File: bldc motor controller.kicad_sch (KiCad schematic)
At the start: 56 parts, among them J1 Conn_01x04_Pin, U1 C47023655, U2 ISM330DHCXTR, U3 C529358, U6 LIS2MDLTR

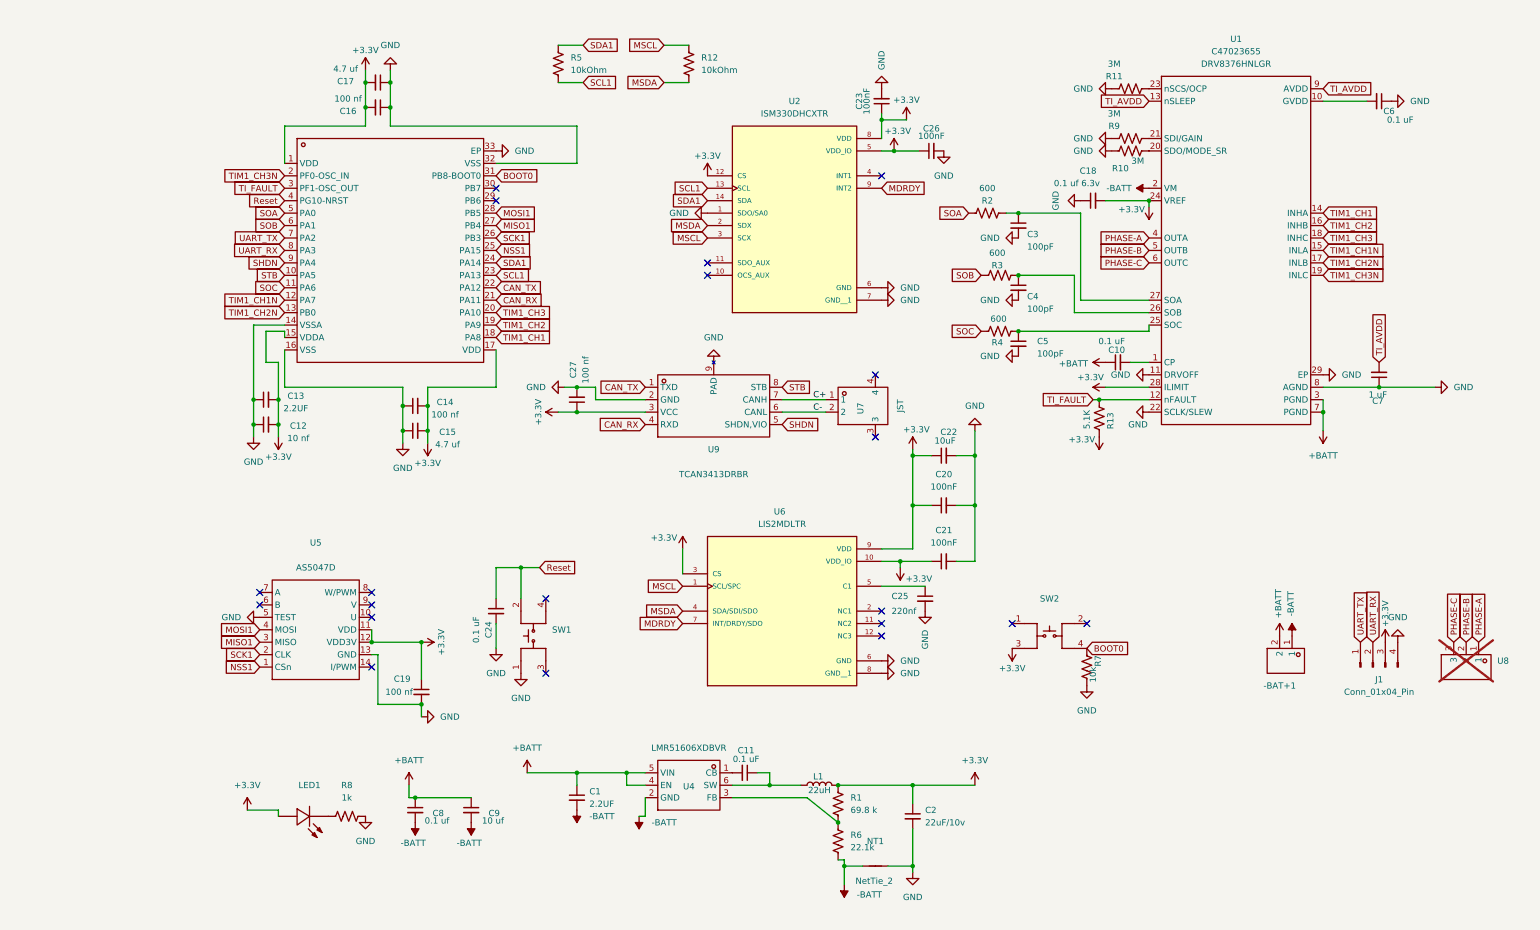
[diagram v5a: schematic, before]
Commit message: updated to min capacitor size and increased width of 3.3v rail
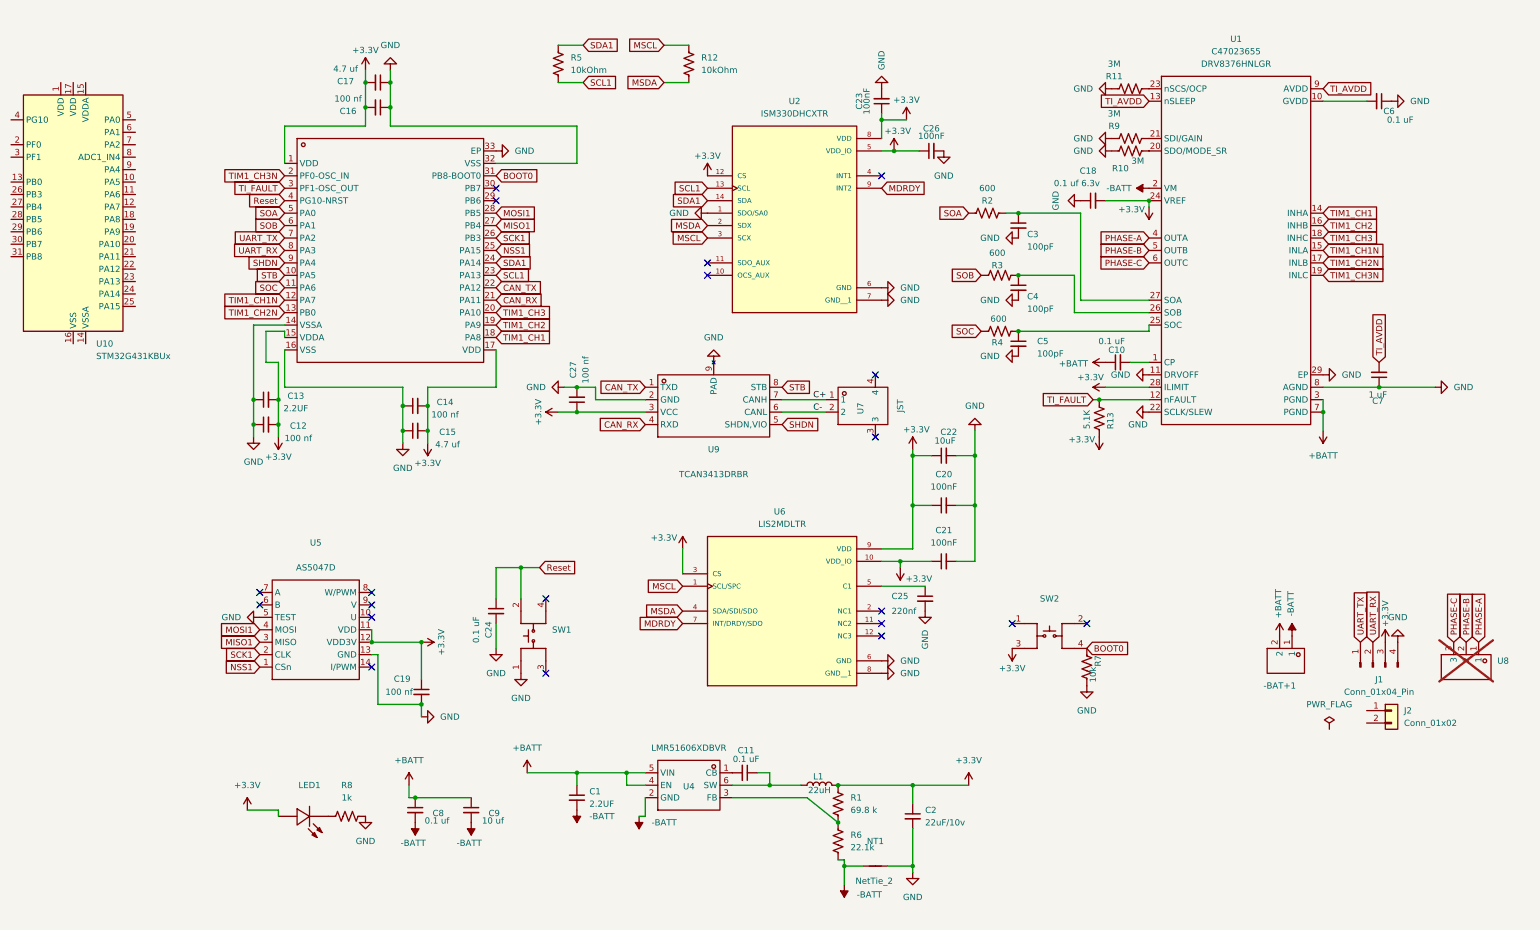
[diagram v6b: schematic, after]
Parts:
- added J2: Conn_01x02, symbol Connector_Generic:Conn_01x02
- added U10: STM32G431KBUx, Package_DFN_QFN:QFN-32-1EP_5x5mm_P0.5mm_EP3.45x3.45mm, symbol MCU_ST_STM32G4:STM32G431KBUx
- C12: value 10 nf -> 100 nf; footprint Capacitor_SMD:C_01005_0402Metric -> Capacitor_SMD:C_0201_0603Metric
- C14, C16, C19, C20, C21, C23, C26, C27, C3, C4, C5: footprint Capacitor_SMD:C_01005_0402Metric -> Capacitor_SMD:C_0201_0603Metric
- C25: footprint Capacitor_SMD:C_01005_0402Metric -> Capacitor_SMD:C_0402_1005Metric
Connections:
- new net: U10.16 (VSS), U10.32 (VSS), U10.33 (VSS)

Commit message: 3.3v plane, finale besides that
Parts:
- removed -BAT+1: ~, Connector_JST:JST_EH_B2B-EH-A_1x02_P2.50mm_Vertical, symbol bldc controller:WAFER-XH254WZ-2AM
- removed U2: ISM330DHCXTR, bldc-motor-footprints:PQFN50P250X300X86-14N, symbol bldc controller:ISM330DHCXTR
- removed U3: C529358, bldc-motor-footprints:QFN-32_L5.0-W5.0-P0.50-BL-EP3.7, symbol bldc controller:STM32G431KBU6
- added C28, C29, C30: 10 uf, Capacitor_SMD:C_0603_1608Metric, symbol Device:C_Small
- added U2: LSM6DSV16XTR, LGA-14L_STM, symbol bldc controller:LSM6DSV16XTR
- J2: footprint (none) -> Connector_JST:JST_EH_B2B-EH-A_1x02_P2.50mm_Vertical
- U1: value C47023655 -> ~; footprint bldc-motor-footprints:VQFN-28_L6.0-W5.0-P0.50-TL-EP4.0 -> ProLib_pcs_2025-10-01 (1):VQFN-28_L6.0-W5.0-P0.50-TL-EP4.0
- U4: footprint bldc-motor-footprints:SOT-23-6_L2.9-W1.6-P0.95-LS2.8-BR -> 48v-3.3v buck:SOT-23-6_L2.9-W1.6-P0.95-LS2.8-BR
- U6: footprint bldc-motor-footprints:PQFN50P200X200X70-12N -> LIS2MDLTR:PQFN50P200X200X70-12N
- U9: footprint bldc-motor-footprints:SON-8_L3.0-W3.0-P0.65-LS2.9-BL-EP -> ProLib_pcs_2025-10-16 (2):SON-8_L3.0-W3.0-P0.65-LS2.9-BL-EP
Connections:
- net +3.3V: now also U10.1 (VDD), U10.15 (VDDA), U10.17 (VDD), U2.12 (CS), U2.5 (VDD_IO), U2.8 (VDD)
- net +BATT: now also J2.2 (Pin_2), C28.1, C29.1, C30.1
- net -BATT: now also J2.1 (Pin_1), C28.2, C29.2, C30.2
- net BOOT0: now also U10.31 (PB8)
- net CAN_RX: now also U10.21 (PA11)
- net CAN_TX: now also U10.22 (PA12)
- net GND: now also U10.14 (VSSA), U10.16 (VSS), U10.32 (VSS), U10.33 (VSS), U2.1 (SDO/SA0), U2.6 (GND), U2.7 (GND)
- net MDRDY: now also U2.9 (INT2)
- net MISO1: now also U10.27 (PB4)
- net MOSI1: now also U10.28 (PB5)
- net MSCL: now also U2.3 (SCX/AH2/QVAR2)
- net MSDA: now also U2.2 (SDX/AH1/QVAR1)
- net NSS1: now also U10.25 (PA15)
- net Reset: now also U10.4 (PG10)
- net SCK1: now also U10.26 (PB3)
- net SCL1: now also U10.23 (PA13), U2.13 (SCL)
- net SDA1: now also U10.24 (PA14), U2.14 (SDA)
- net SHDN: now also U10.9 (PA4)
- net SOA: now also U10.5 (PA0)
- net SOB: now also U10.6 (PA1)
- net SOC: now also U10.11 (PA6)
- net STB: now also U10.10 (PA5)
- net TIM1_CH1: now also U10.18 (PA8)
- net TIM1_CH1N: now also U10.12 (PA7)
- net TIM1_CH2: now also U10.19 (PA9)
- net TIM1_CH2N: now also U10.13 (PB0)
- net TIM1_CH3: now also U10.20 (PA10)
- net TIM1_CH3N: now also U10.2 (PF0)
- net TI_FAULT: now also U10.3 (PF1)
- net UART_RX: now also U10.8 (PA3)
- net UART_TX: now also U10.7 (PA2)
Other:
- moved on the sheet: C12, C13, C14, C15, C16, C17, C23, C26, C27, C8, C9, J2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

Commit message: final review time
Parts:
- J1: now not fitted
- R12, R5: value 10kOhm -> 10k
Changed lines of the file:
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@@
 			)
 		)
-		(property "Value" "10kOhm"
+		(property "Value" "10k"
 			(at 105.41 38.0999 0)
 			(effects
@@
 		(in_bom yes)
 		(on_board yes)
-		(dnp no)
+		(dnp yes)
 		(fields_autoplaced yes)
 		(property "Reference" "J1"
@@
 			)
 		)
-		(property "Value" "10kOhm"
+		(property "Value" "10k"
 			(at 132.08 38.0999 0)
 			(effects
@@
 		)
 		(pin "8"
-			(alternate "LPUART1_RX")
+			(alternate "USART2_RX")
 		)
 		(pin "13"
@@
 		)
 		(pin "7"
-			(alternate "LPUART1_TX")
+			(alternate "USART2_TX")
 		)
 		(pin "18"
